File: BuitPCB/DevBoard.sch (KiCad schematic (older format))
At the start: 1 part, among them U1 Teensy4.1

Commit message: Added most of components, few pending
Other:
- moved on the sheet: U1
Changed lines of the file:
@@
 $Descr A4 11693 8268
 encoding utf-8
-Sheet 2 4
+Sheet 2 5
 Title ""
 Date ""
@@
 L teensy:Teensy4.1 U?
 U 1 1 61A96076
-P 5800 4050
+P 6050 4000
 AR Path="/61A96076" Ref="U?"  Part="1"
 AR Path="/61A90B8E/61A96076" Ref="U1"  Part="1"
-F 0 "U1" H 5800 6615 50  0000 C CNN
-F 1 "Teensy4.1" H 5800 6524 50  0000 C CNN
-F 2 "teensy:Teensy41" H 5400 4450 50  0001 C CNN
-F 3 "" H 5400 4450 50  0001 C CNN
-	1    5800 4050
+F 0 "U1" H 6050 6565 50  0000 C CNN
+F 1 "Teensy4.1" H 6050 6474 50  0000 C CNN
+F 2 "teensy:Teensy41" H 5650 4400 50  0001 C CNN
+F 3 "" H 5650 4400 50  0001 C CNN
+	1    6050 4000
 	1    0    0    -1
 $EndComp
@@
 L power:GND #PWR0101
 U 1 1 61A9C991
-P 4700 1900
-F 0 "#PWR0101" H 4700 1650 50  0001 C CNN
-F 1 "GND" V 4705 1772 50  0000 R CNN
-F 2 "" H 4700 1900 50  0001 C CNN
-F 3 "" H 4700 1900 50  0001 C CNN
-	1    4700 1900
+P 4950 1850
+F 0 "#PWR0101" H 4950 1600 50  0001 C CNN
+F 1 "GND" V 4955 1722 50  0000 R CNN
+F 2 "" H 4950 1850 50  0001 C CNN
+F 3 "" H 4950 1850 50  0001 C CNN
+	1    4950 1850
 	0    1    1    0
 $EndComp
@@
 L power:GND #PWR0102
 U 1 1 61A9CF3F
-P 5800 5350
-F 0 "#PWR0102" H 5800 5100 50  0001 C CNN
-F 1 "GND" H 5805 5177 50  0000 C CNN
-F 2 "" H 5800 5350 50  0001 C CNN
-F 3 "" H 5800 5350 50  0001 C CNN
-	1    5800 5350
+P 6050 5300
+F 0 "#PWR0102" H 6050 5050 50  0001 C CNN
+F 1 "GND" H 6055 5127 50  0000 C CNN
+F 2 "" H 6050 5300 50  0001 C CNN
+F 3 "" H 6050 5300 50  0001 C CNN
+	1    6050 5300
 	1    0    0    -1
 $EndComp
@@
 L power:GND #PWR0103
 U 1 1 61A9EF5C
-P 4700 4950
-F 0 "#PWR0103" H 4700 4700 50  0001 C CNN
-F 1 "GND" V 4705 4822 50  0000 R CNN
-F 2 "" H 4700 4950 50  0001 C CNN
-F 3 "" H 4700 4950 50  0001 C CNN
-	1    4700 4950
+P 4950 4900
+F 0 "#PWR0103" H 4950 4650 50  0001 C CNN
+F 1 "GND" V 4955 4772 50  0000 R CNN
+F 2 "" H 4950 4900 50  0001 C CNN
+F 3 "" H 4950 4900 50  0001 C CNN
+	1    4950 4900
 	0    1    1    0
 $EndComp
@@
 L power:GND #PWR0104
 U 1 1 61A9F9EA
-P 4700 5050
-F 0 "#PWR0104" H 4700 4800 50  0001 C CNN
-F 1 "GND" V 4705 4922 50  0000 R CNN
-F 2 "" H 4700 5050 50  0001 C CNN
-F 3 "" H 4700 5050 50  0001 C CNN
-	1    4700 5050
+P 4950 5000
+F 0 "#PWR0104" H 4950 4750 50  0001 C CNN
+F 1 "GND" V 4955 4872 50  0000 R CNN
+F 2 "" H 4950 5000 50  0001 C CNN
+F 3 "" H 4950 5000 50  0001 C CNN
+	1    4950 5000
 	0    1    1    0
 $EndComp
@@
 L power:GND #PWR0105
 U 1 1 61A9FFE0
-P 6900 3300
-F 0 "#PWR0105" H 6900 3050 50  0001 C CNN
-F 1 "GND" V 6905 3172 50  0000 R CNN
-F 2 "" H 6900 3300 50  0001 C CNN
-F 3 "" H 6900 3300 50  0001 C CNN
-	1    6900 3300
+P 7150 3250
+F 0 "#PWR0105" H 7150 3000 50  0001 C CNN
+F 1 "GND" V 7155 3122 50  0000 R CNN
+F 2 "" H 7150 3250 50  0001 C CNN
+F 3 "" H 7150 3250 50  0001 C CNN
+	1    7150 3250
 	0    -1   -1   0
 $EndComp
@@
 L power:GND #PWR0106
 U 1 1 61AA08C4
-P 6900 2000
-F 0 "#PWR0106" H 6900 1750 50  0001 C CNN
-F 1 "GND" V 6905 1872 50  0000 R CNN
-F 2 "" H 6900 2000 50  0001 C CNN
-F 3 "" H 6900 2000 50  0001 C CNN
-	1    6900 2000
+P 7150 1950
+F 0 "#PWR0106" H 7150 1700 50  0001 C CNN
+F 1 "GND" V 7155 1822 50  0000 R CNN
+F 2 "" H 7150 1950 50  0001 C CNN
+F 3 "" H 7150 1950 50  0001 C CNN
+	1    7150 1950
 	0    -1   -1   0
 $EndComp
@@
 L power:GND #PWR0107
 U 1 1 61AA1181
-P 6900 4550
-F 0 "#PWR0107" H 6900 4300 50  0001 C CNN
-F 1 "GND" V 6905 4422 50  0000 R CNN
-F 2 "" H 6900 4550 50  0001 C CNN
-F 3 "" H 6900 4550 50  0001 C CNN
-	1    6900 4550
+P 7150 4500
+F 0 "#PWR0107" H 7150 4250 50  0001 C CNN
+F 1 "GND" V 7155 4372 50  0000 R CNN
+F 2 "" H 7150 4500 50  0001 C CNN
+F 3 "" H 7150 4500 50  0001 C CNN
+	1    7150 4500
 	0    -1   -1   0
 $EndComp

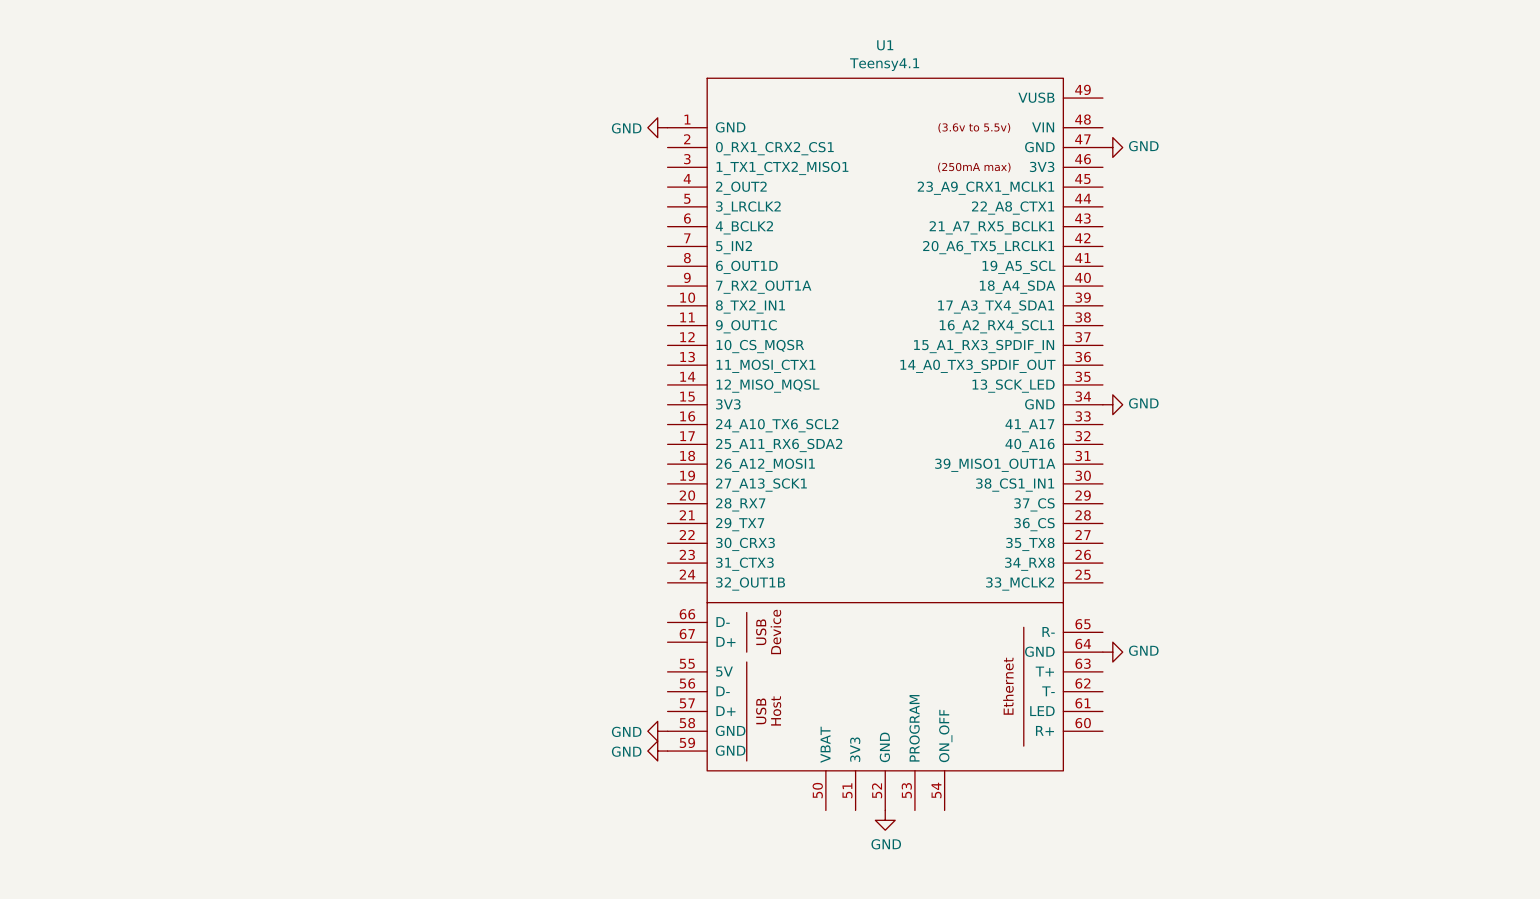
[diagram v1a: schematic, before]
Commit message: Added sensors connectors
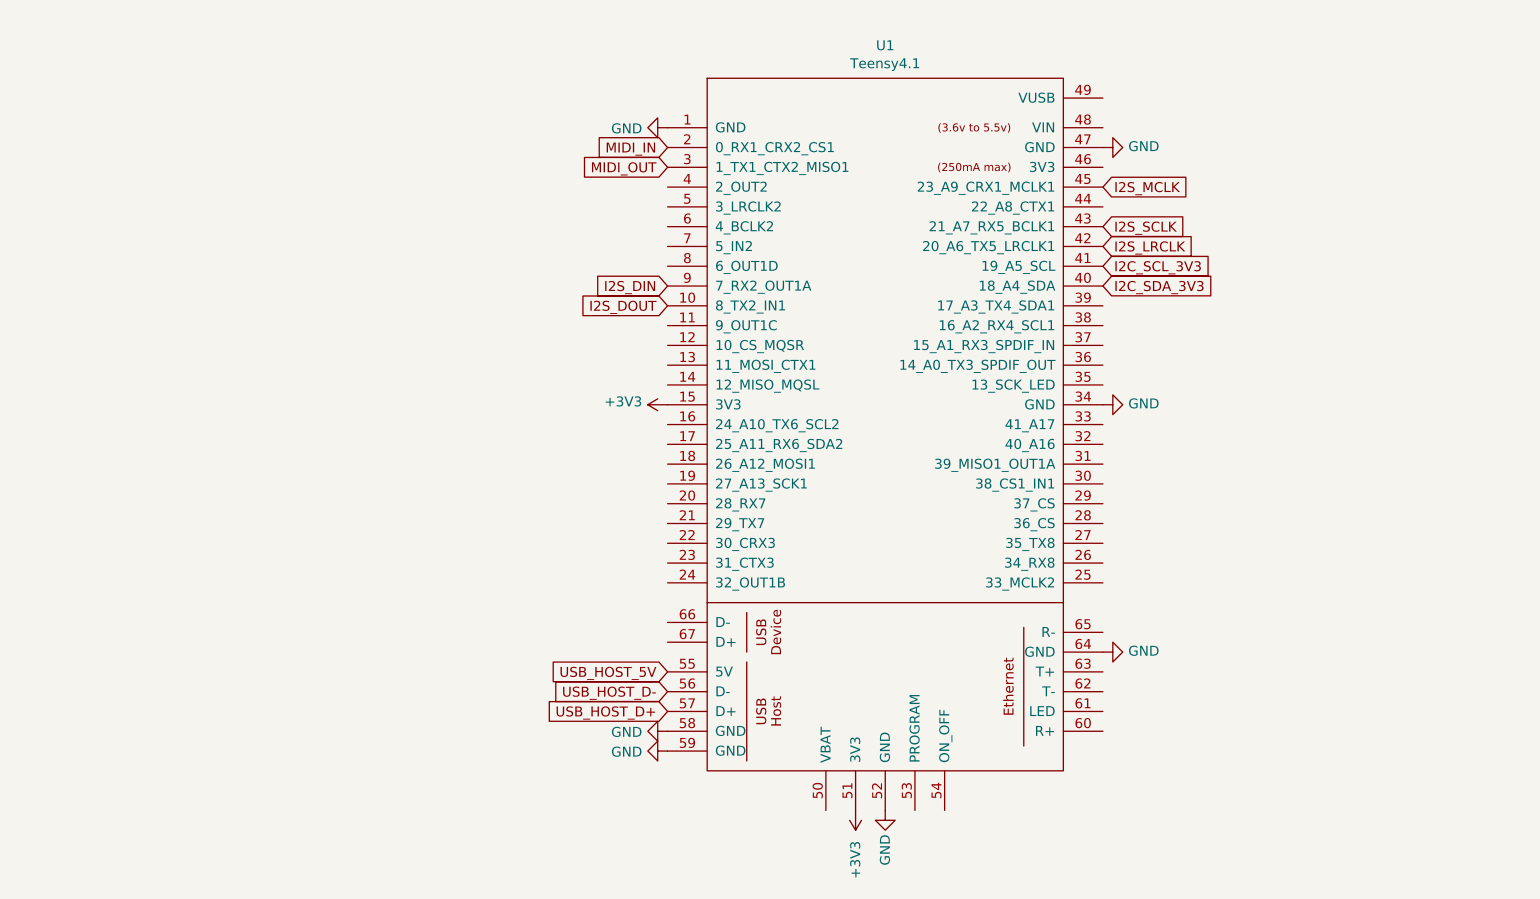
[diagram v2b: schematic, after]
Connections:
- net I2S_DOUT: now reaches U1.10 (8_TX2_IN1)
- net +3V3: now reaches U1.15 (3V3)
- net +3V3: now also U1.51 (3V3)
- net MIDI_IN: now reaches U1.2 (0_RX1_CRX2_CS1)
- net MIDI_OUT: now reaches U1.3 (1_TX1_CTX2_MISO1)
- net I2C_SDA_3V3: now reaches U1.40 (18_A4_SDA)
- net I2C_SCL_3V3: now reaches U1.41 (19_A5_SCL)
- net I2S_LRCLK: now reaches U1.42 (20_A6_TX5_LRCLK1)
- net I2S_SCLK: now reaches U1.43 (21_A7_RX5_BCLK1)
- net I2S_MCLK: now reaches U1.45 (23_A9_CRX1_MCLK1)
- net USB_HOST_5V: now reaches U1.55 (5V)
- net USB_HOST_D-: now reaches U1.56 (D-)
- net USB_HOST_D+: now reaches U1.57 (D+)
- net I2S_DIN: now reaches U1.9 (7_RX2_OUT1A)
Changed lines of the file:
@@
 $Descr A4 11693 8268
 encoding utf-8
-Sheet 2 5
+Sheet 2 6
 Title ""
 Date ""
@@
 P 6050 5300
 F 0 "#PWR0102" H 6050 5050 50  0001 C CNN
-F 1 "GND" H 6055 5127 50  0000 C CNN
+F 1 "GND" V 6050 5100 50  0000 C CNN
 F 2 "" H 6050 5300 50  0001 C CNN
 F 3 "" H 6050 5300 50  0001 C CNN
@@
 	0    -1   -1   0
 $EndComp
+Text GLabel 4950 4800 0    50   Input ~ 0
+USB_HOST_D+
+Text GLabel 4950 4700 0    50   Input ~ 0
+USB_HOST_D-
+$Comp
+L power:+3V3 #PWR0108
+U 1 1 61AB5F49
+P 4950 3250
+F 0 "#PWR0108" H 4950 3100 50  0001 C CNN
+F 1 "+3V3" V 4965 3378 50  0000 L CNN
+F 2 "" H 4950 3250 50  0001 C CNN
+F 3 "" H 4950 3250 50  0001 C CNN
+	1    4950 3250
+	0    -1   -1   0
+$EndComp
+$Comp
+L power:+3V3 #PWR0109
+U 1 1 61AB6DCC
+P 5900 5300
+F 0 "#PWR0109" H 5900 5150 50  0001 C CNN
+F 1 "+3V3" V 5900 5550 50  0000 C CNN
+F 2 "" H 5900 5300 50  0001 C CNN
+F 3 "" H 5900 5300 50  0001 C CNN
+	1    5900 5300
+	-1   0    0    1
+$EndComp
+Text GLabel 4950 4600 0    50   Input ~ 0
+USB_HOST_5V
+Text GLabel 7150 2650 2    50   Input ~ 0
+I2C_SDA_3V3
+Text GLabel 7150 2550 2    50   Input ~ 0
+I2C_SCL_3V3
+Text GLabel 7150 2150 2    50   Input ~ 0
+I2S_MCLK
+Text GLabel 7150 2450 2    50   Input ~ 0
+I2S_LRCLK
+Text GLabel 4950 2750 0    50   Input ~ 0
+I2S_DOUT
+Text GLabel 4950 2650 0    50   Input ~ 0
+I2S_DIN
+Text GLabel 7150 2350 2    50   Input ~ 0
+I2S_SCLK
+Text GLabel 4950 1950 0    50   Input ~ 0
+MIDI_IN
+Text GLabel 4950 2050 0    50   Input ~ 0
+MIDI_OUT
 $EndSCHEMATC

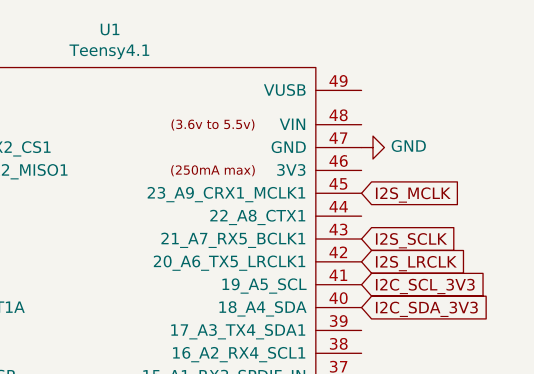
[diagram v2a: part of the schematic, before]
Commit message: Updated adding battery management sheet and componnents to PCB
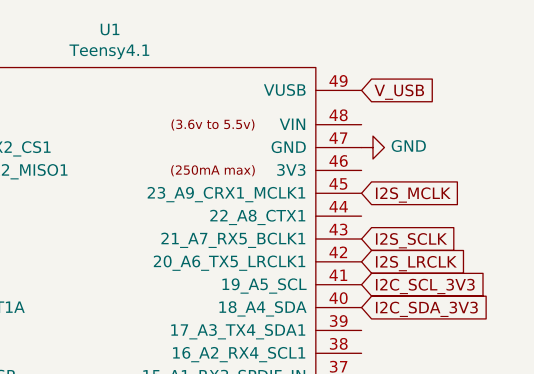
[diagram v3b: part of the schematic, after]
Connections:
- net V_USB: now reaches U1.49 (VUSB)
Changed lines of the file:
@@
 $Descr A4 11693 8268
 encoding utf-8
-Sheet 2 6
+Sheet 2 7
 Title ""
 Date ""
@@
 Text GLabel 4950 2050 0    50   Input ~ 0
 MIDI_OUT
+Text GLabel 7150 1700 2    50   Input ~ 0
+V_USB
 $EndSCHEMATC
